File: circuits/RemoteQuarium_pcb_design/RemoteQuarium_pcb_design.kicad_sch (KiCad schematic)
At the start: 18 parts, among them J1 Power_terminal, J10 LCD_pins, J11 Feeder_servo_pins, J12 ESP_pins, J13 TX_RX, J15 Ph_sensor_sockets, J2 ESP left side sockets, J3 ESP right side sockets, J4 Relay_terminal, J6 Temp_sensor_socket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

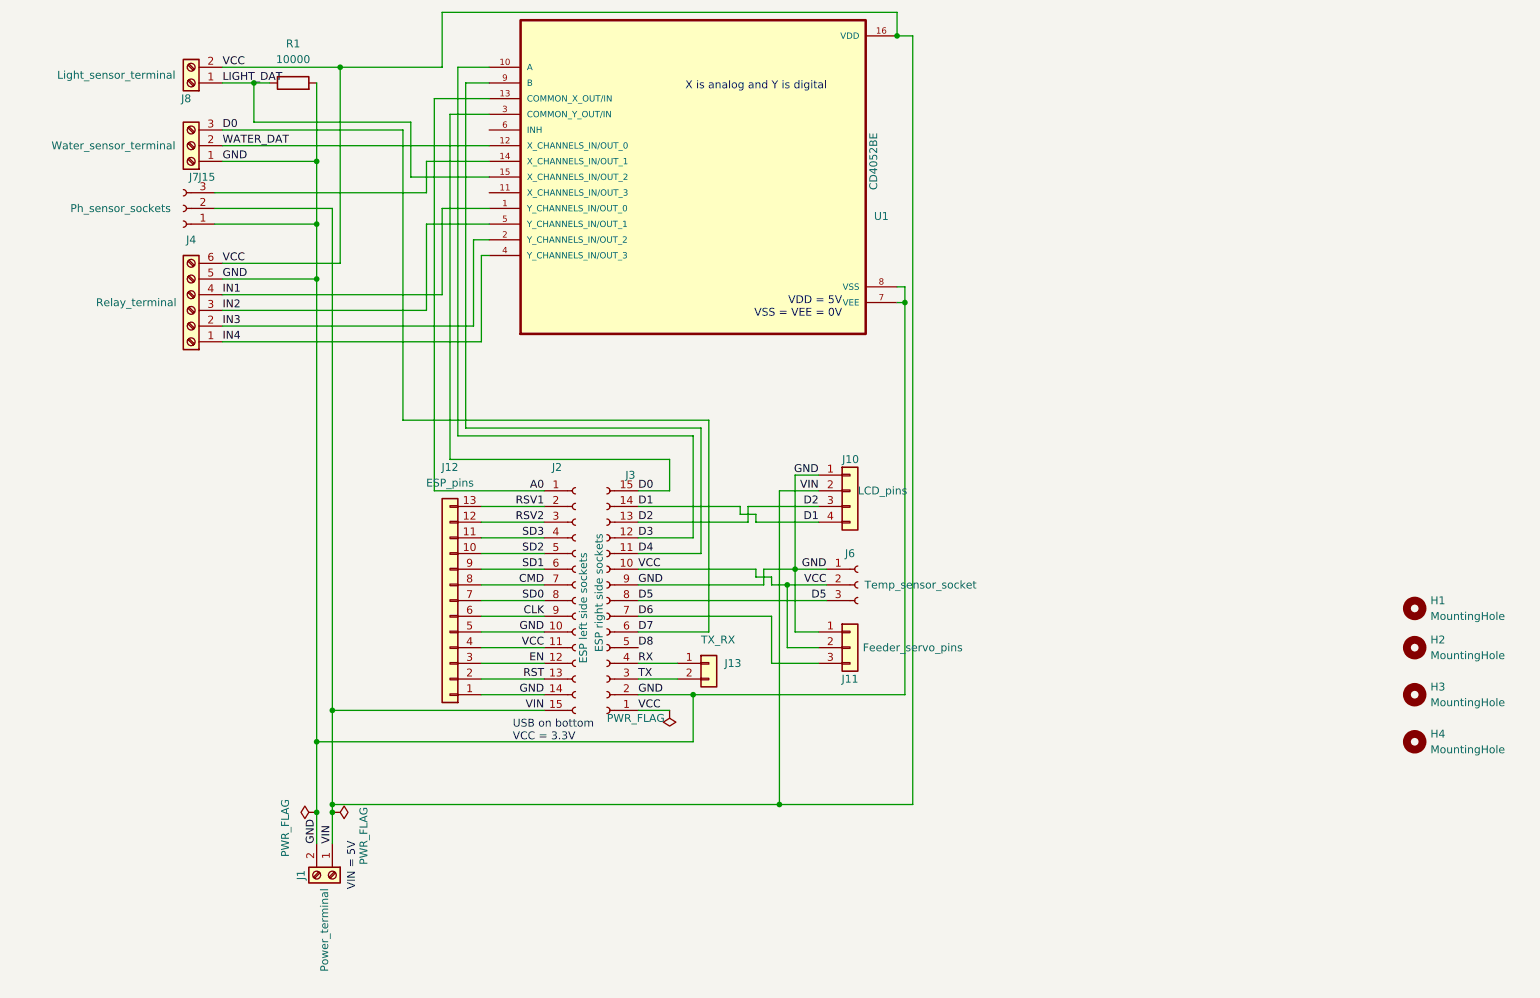
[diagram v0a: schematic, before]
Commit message: Php api files are ready DB tables created, models are ok, DAO interface implemented and DAO is ready without function implementations. Controls are remaining.
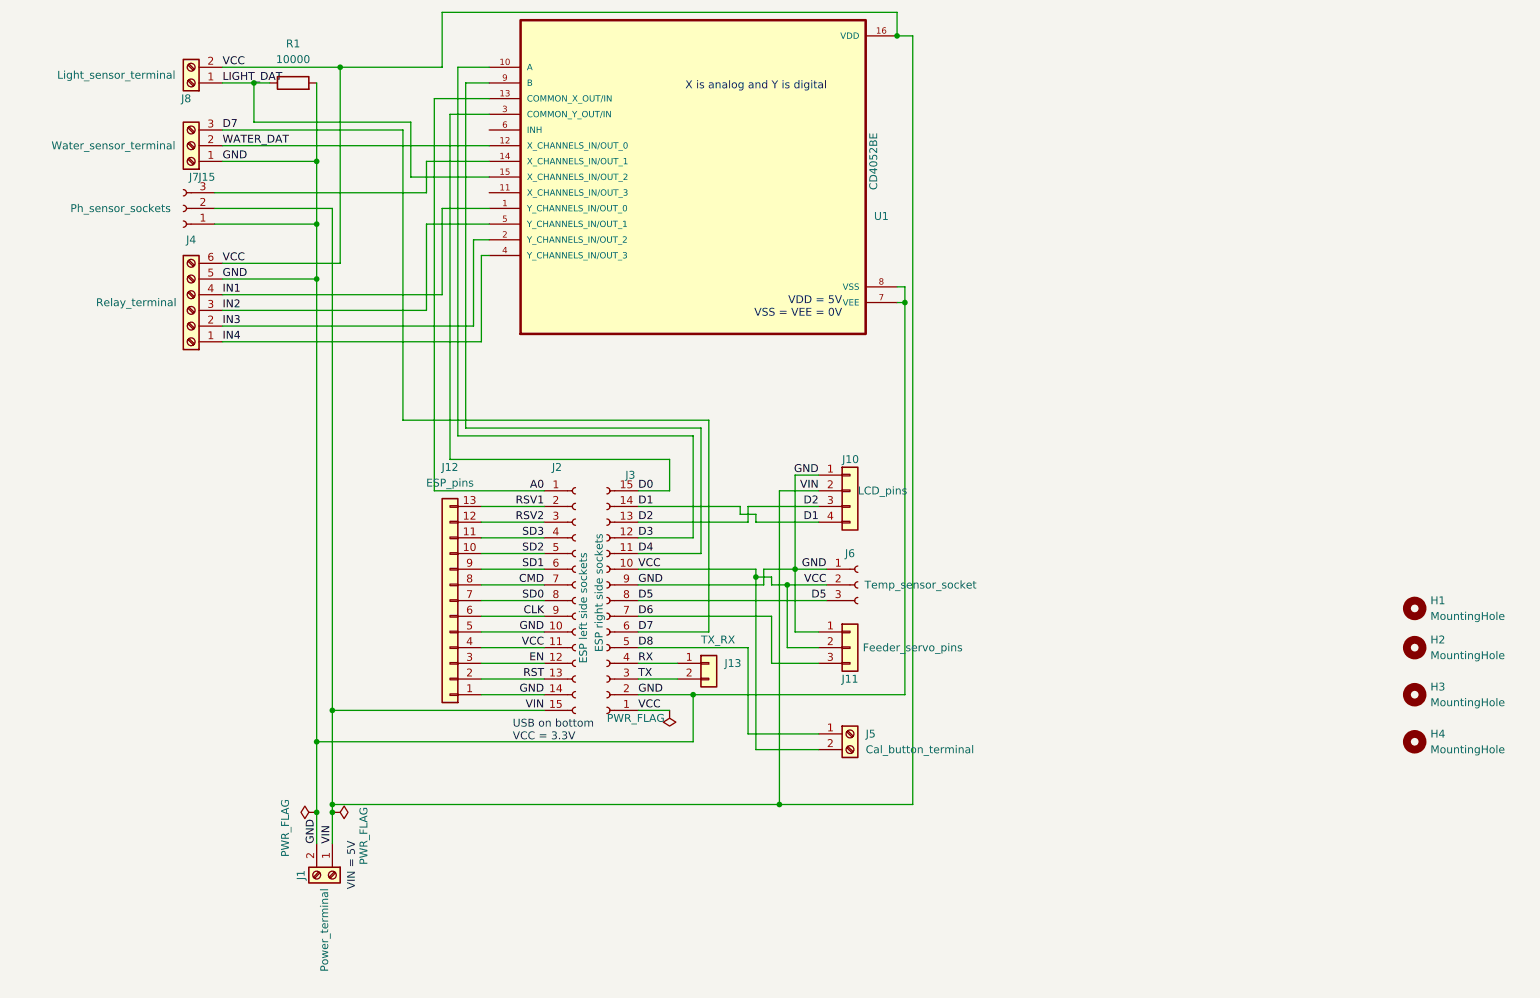
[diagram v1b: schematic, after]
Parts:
- added J5: Cal_button_terminal, symbol Connector:Screw_Terminal_01x02
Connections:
- net D0: no longer J3.6 (Pin_6), J7.3 (Pin_3)
- net D8: now also J5.1 (Pin_1)
- net VCC: now also J5.2 (Pin_2)
- new net D7: J3.6 (Pin_6), J7.3 (Pin_3)
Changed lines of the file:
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@@
   (junction (at 83.82 147.32) (diameter 0) (color 0 0 0 0)
   )
+  (junction (at 152.4 109.22) (diameter 0) (color 0 0 0 0)
+  )
   (junction (at 81.28 147.32) (diameter 0) (color 0 0 0 0)
   )
@@
     (stroke (width 0) (type default))
   )
+  (wire (pts (xy 162.56 137.16) (xy 152.4 137.16))
+    (stroke (width 0) (type default))
+  )
   (wire (pts (xy 107.95 97.79) (xy 118.11 97.79))
     (stroke (width 0) (type default))
@@
     (stroke (width 0) (type default))
   )
+  (wire (pts (xy 162.56 134.62) (xy 151.13 134.62))
+    (stroke (width 0) (type default))
+  )
   (wire (pts (xy 143.51 105.41) (xy 133.35 105.41))
     (stroke (width 0) (type default))
@@
     (stroke (width 0) (type default))
   )
+  (wire (pts (xy 152.4 109.22) (xy 152.4 137.16))
+    (stroke (width 0) (type default))
+  )
   (wire (pts (xy 99.06 46.99) (xy 99.06 41.91))
     (stroke (width 0) (type default))
@@
     (stroke (width 0) (type default))
   )
+  (wire (pts (xy 151.13 134.62) (xy 151.13 120.65))
+    (stroke (width 0) (type default))
+  )
   (wire (pts (xy 107.95 102.87) (xy 118.11 102.87))
     (stroke (width 0) (type default))
@@
     (stroke (width 0) (type default))
   )
+  (wire (pts (xy 151.13 120.65) (xy 133.35 120.65))
+    (stroke (width 0) (type default))
+  )
   (wire (pts (xy 162.56 118.11) (xy 158.75 118.11))
     (stroke (width 0) (type default))
@@
     (effects (font (size 1.27 1.27)) (justify left bottom))
   )
-  (label "D0" (at 66.04 36.83 0) (fields_autoplaced)
+  (label "D7" (at 66.04 36.83 0) (fields_autoplaced)
     (effects (font (size 1.27 1.27)) (justify left bottom))
   )
@@
         )
       )
+    )
+  )
+  (symbol (lib_id "Connector:Screw_Terminal_01x02") (at 167.64 134.62 0) (unit 1)
+    (in_bom yes) (on_board yes) (dnp no) (fields_autoplaced)
+    (property "Reference" "J5" (at 170.18 134.62 0)
+      (effects (font (size 1.27 1.27)) (justify left))
+    )
+    (property "Value" "Cal_button_terminal" (at 170.18 137.16 0)
+      (effects (font (size 1.27 1.27)) (justify left))
+    )
+    (property "Footprint" "" (at 167.64 134.62 0)
+      (effects (font (size 1.27 1.27)) hide)
+    )
+    (property "Datasheet" "~" (at 167.64 134.62 0)
+      (effects (font (size 1.27 1.27)) hide)
+    )
+    (pin "1")
+    (pin "2")
+    (instances
+      (project "RemoteQuarium_pcb_design"
+        (path "/60f012de-ecaa-41fb-b4e2-f0417ffff4b9"
+          (reference "J5") (unit 1)
+        )
+      )

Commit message: ESP confg update is working, ready to do actuators and sensor data porting. PH sensor is reading contant data IDK why..
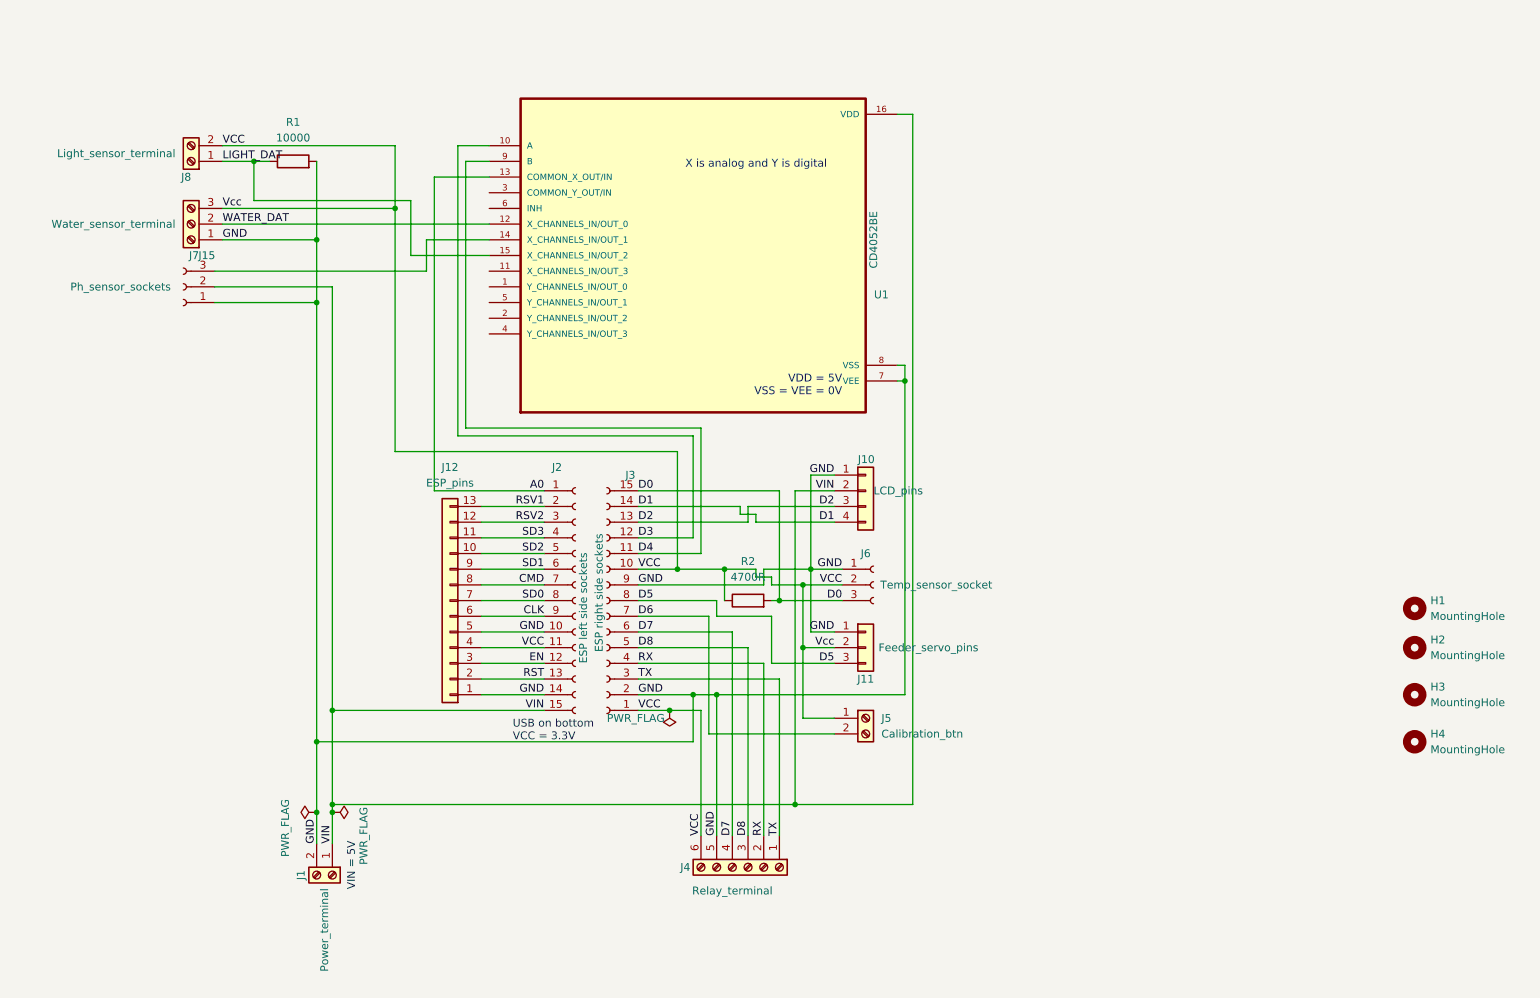
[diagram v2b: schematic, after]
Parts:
- removed J13: TX_RX, Connector_PinHeader_2.54mm:PinHeader_1x02_P2.54mm_Vertical, symbol Connector_Generic:Conn_01x02
- added R2: 4700R, symbol Device:R
- J5: value Cal_button_terminal -> Calibration_btn
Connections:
- net D0: now also J6.3 (Pin_3), R2.2; no longer U1.3 (COMMON_Y_OUT/IN)
- net D5: now also J11.3 (Pin_3); no longer J6.3 (Pin_3)
- net D6: now also J5.2 (Pin_2); no longer J11.3 (Pin_3)
- net D7: now also J4.4 (Pin_4); no longer J7.3 (Pin_3)
- net D8: now also J4.3 (Pin_3); no longer J5.1 (Pin_1)
- net RX: now also J4.2 (Pin_2)
- net TX: now also J4.1 (Pin_1)
- net VCC: now also J5.1 (Pin_1), J7.3 (Pin_3), R2.1; no longer J1.1 (Pin_1), J10.2 (Pin_2), J15.2 (Pin_2), J2.15 (Pin_15), J5.2 (Pin_2), U1.16 (VDD)
- net IN1: no longer names the net of U1.1 (Y_CHANNELS_IN/OUT_0)
- net IN1: no longer J4.4 (Pin_4)
- net IN2: no longer names the net of U1.5 (Y_CHANNELS_IN/OUT_1)
- net IN2: no longer J4.3 (Pin_3)
- net IN3: no longer names the net of U1.2 (Y_CHANNELS_IN/OUT_2)
- net IN3: no longer J4.2 (Pin_2)
- net IN4: no longer names the net of U1.4 (Y_CHANNELS_IN/OUT_3)
- net IN4: no longer J4.1 (Pin_1)
- new net VIN: J1.1 (Pin_1), J10.2 (Pin_2), J15.2 (Pin_2), J2.15 (Pin_15), U1.16 (VDD)
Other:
- moved on the sheet: J10, J11, J15, J4, J6, J7, J8, R1, U1

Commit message: Made PCB plans, it should be double checked but seems ok. Added basic info display to code tested!
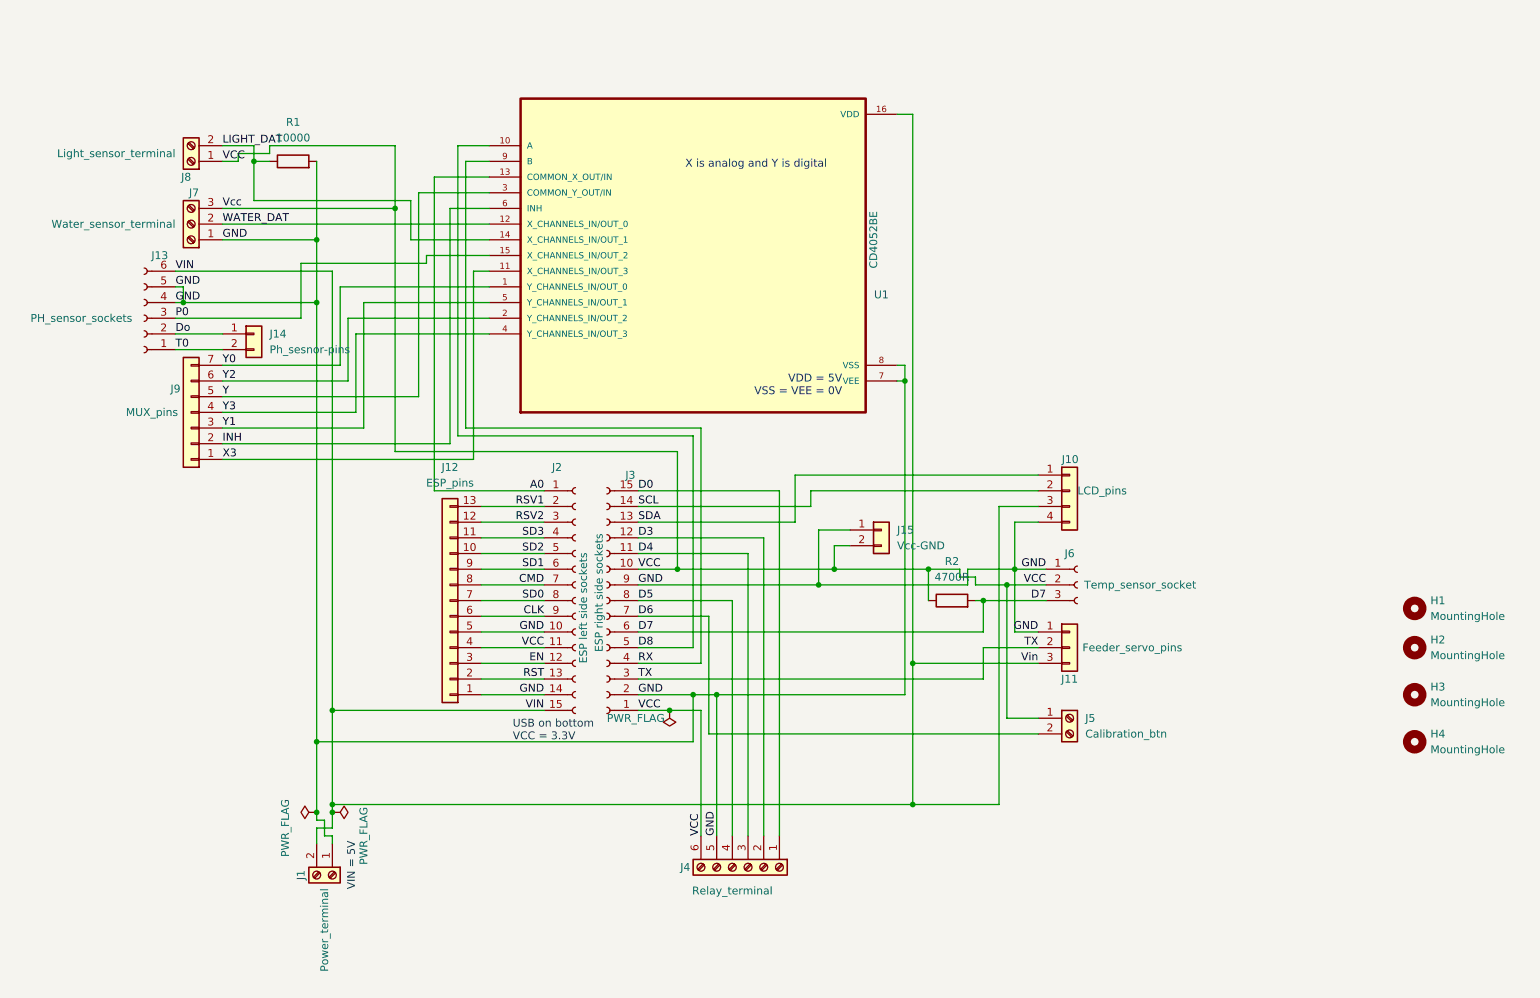
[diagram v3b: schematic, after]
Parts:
- removed J15: Ph_sensor_sockets, symbol Connector:Conn_01x03_Socket
- added J13: PH_sensor_sockets, Connector_PinSocket_2.54mm:PinSocket_1x06_P2.54mm_Horizontal, symbol Connector:Conn_01x06_Socket
- added J14: Ph_sesnor-pins, Connector_PinHeader_2.54mm:PinHeader_1x02_P2.54mm_Vertical, symbol Connector_Generic:Conn_01x02
- added J15: Vcc-GND, Connector_PinHeader_2.54mm:PinHeader_1x02_P2.54mm_Vertical, symbol Connector_Generic:Conn_01x02
- added J9: MUX_pins, Connector_PinHeader_2.54mm:PinHeader_1x07_P2.54mm_Vertical, symbol Connector_Generic:Conn_01x07
- J11: footprint (none) -> Connector_PinHeader_2.54mm:PinHeader_1x03_P2.54mm_Vertical
- J5: footprint (none) -> TerminalBlock_Phoenix:TerminalBlock_Phoenix_MPT-0,5-2-2.54_1x02_P2.54mm_Horizontal
- R2: footprint (none) -> Resistor_THT:R_Axial_DIN0204_L3.6mm_D1.6mm_P5.08mm_Horizontal
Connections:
- net D0: now also J4.1 (Pin_1); no longer J6.3 (Pin_3), R2.2
- net D3: now also J4.2 (Pin_2); no longer U1.10 (A)
- net D4: now also J4.3 (Pin_3); no longer U1.9 (B)
- net D5: now also J4.4 (Pin_4); no longer J11.3 (Pin_3)
- net D7: now also J6.3 (Pin_3), R2.2; no longer J4.4 (Pin_4)
- net D8: now also U1.10 (A); no longer J4.3 (Pin_3)
- net GND: now also J1.1 (Pin_1), J10.4 (Pin_4), J13.4 (Pin_4), J13.5 (Pin_5), J15.1 (Pin_1); no longer J1.2 (Pin_2), J10.1 (Pin_1)
- net LIGHT_DAT: now also J8.2 (Pin_2), U1.14 (X_CHANNELS_IN/OUT_1); no longer J8.1 (Pin_1), U1.15 (X_CHANNELS_IN/OUT_2)
- net RX: now also U1.9 (B); no longer J4.2 (Pin_2)
- net TX: now also J11.2 (Pin_2); no longer J4.1 (Pin_1)
- net VCC: now also J8.1 (Pin_1), J15.2 (Pin_2); no longer J11.2 (Pin_2), J8.2 (Pin_2)
- net VIN: now also J1.2 (Pin_2), J10.3 (Pin_3), J11.3 (Pin_3), J13.6 (Pin_6); no longer J1.1 (Pin_1), J10.2 (Pin_2)
- net Y0: now reaches U1.1 (Y_CHANNELS_IN/OUT_0)
- net Y0: now also J9.7 (Pin_7)
- net X3: now reaches U1.11 (X_CHANNELS_IN/OUT_3)
- net X3: now also J9.1 (Pin_1)
- net Y2: now reaches U1.2 (Y_CHANNELS_IN/OUT_2)
- net Y2: now also J9.6 (Pin_6)
- net Y: now reaches U1.3 (COMMON_Y_OUT/IN)
- net Y: now also J9.5 (Pin_5)
- net Y3: now reaches U1.4 (Y_CHANNELS_IN/OUT_3)
- net Y3: now also J9.4 (Pin_4)
- net Y1: now reaches U1.5 (Y_CHANNELS_IN/OUT_1)
- net Y1: now also J9.3 (Pin_3)
- net INH: now reaches U1.6 (INH)
- net INH: now also J9.2 (Pin_2)
- net D1 renamed SCL
- net SCL: now also J10.2 (Pin_2); no longer J10.4 (Pin_4)
- net D2 renamed SDA
- net SDA: now also J10.1 (Pin_1); no longer J10.3 (Pin_3)
- new net Do: J13.2 (Pin_2), J14.1 (Pin_1)
- new net P0: J13.3 (Pin_3), U1.15 (X_CHANNELS_IN/OUT_2)
- new net T0: J13.1 (Pin_1), J14.2 (Pin_2)
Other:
- moved on the sheet: J10, J11, J5, J6, R2
